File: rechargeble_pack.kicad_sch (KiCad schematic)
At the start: 42 parts, among them J1 Out, J2 LiPo, J3 DC IN, Q1 IRLML6402, Q2 BC857, Q6 BC847, Q7 BC857, U1 TP4056, U2 TPS61041

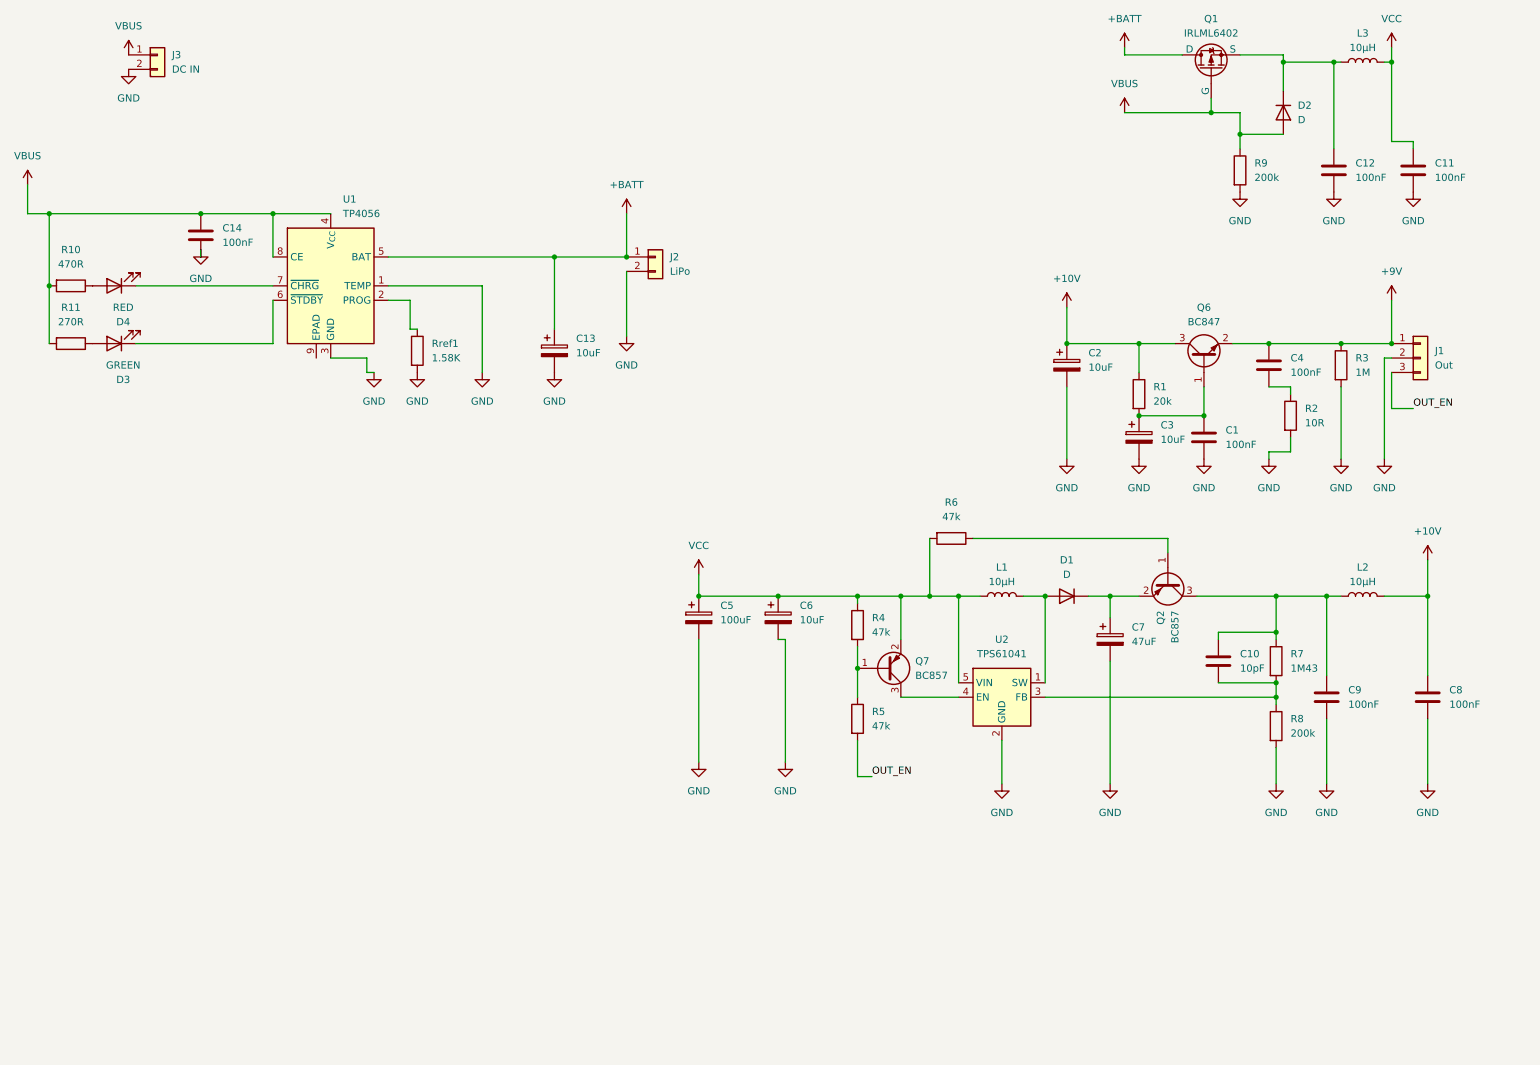
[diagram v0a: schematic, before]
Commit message: v3 redesign: 31x19 mm one-sided board, regulated 9.0 V, single LED
- Charger TP4057 (500 mA), power-path removed, MLCC instead of tantalum
- Boost TPS61041 at 11.5 V with output disconnect (Q2), EN pull-down fix
- Output chain: RC -> capacitance multiplier -> TPS7A4901 ultra-low-noise LDO, 9.02 V
- Single red/green LED: charging / charged / blinking low-battery (TLV3012)
- USB-C input TVS, project symbol library, JLC basic parts where possible
- New layout 31x19 mm, 2 layers, all SMD on top, ABYSS logo on bottom silk
- production/: gerbers, BOM+CPL for JLCPCB and PCBWay
- README rewritten, .gitignore added, v1 gerbers/BOM/CPL, KiCad backups and caches removed

Co-Authored-By: Claude Opus 5.5 <noreply@anthropic.com>
Claude-Session: https://claude.ai/code/session_01MaiZSNzApBdaqcYQCa8rQi
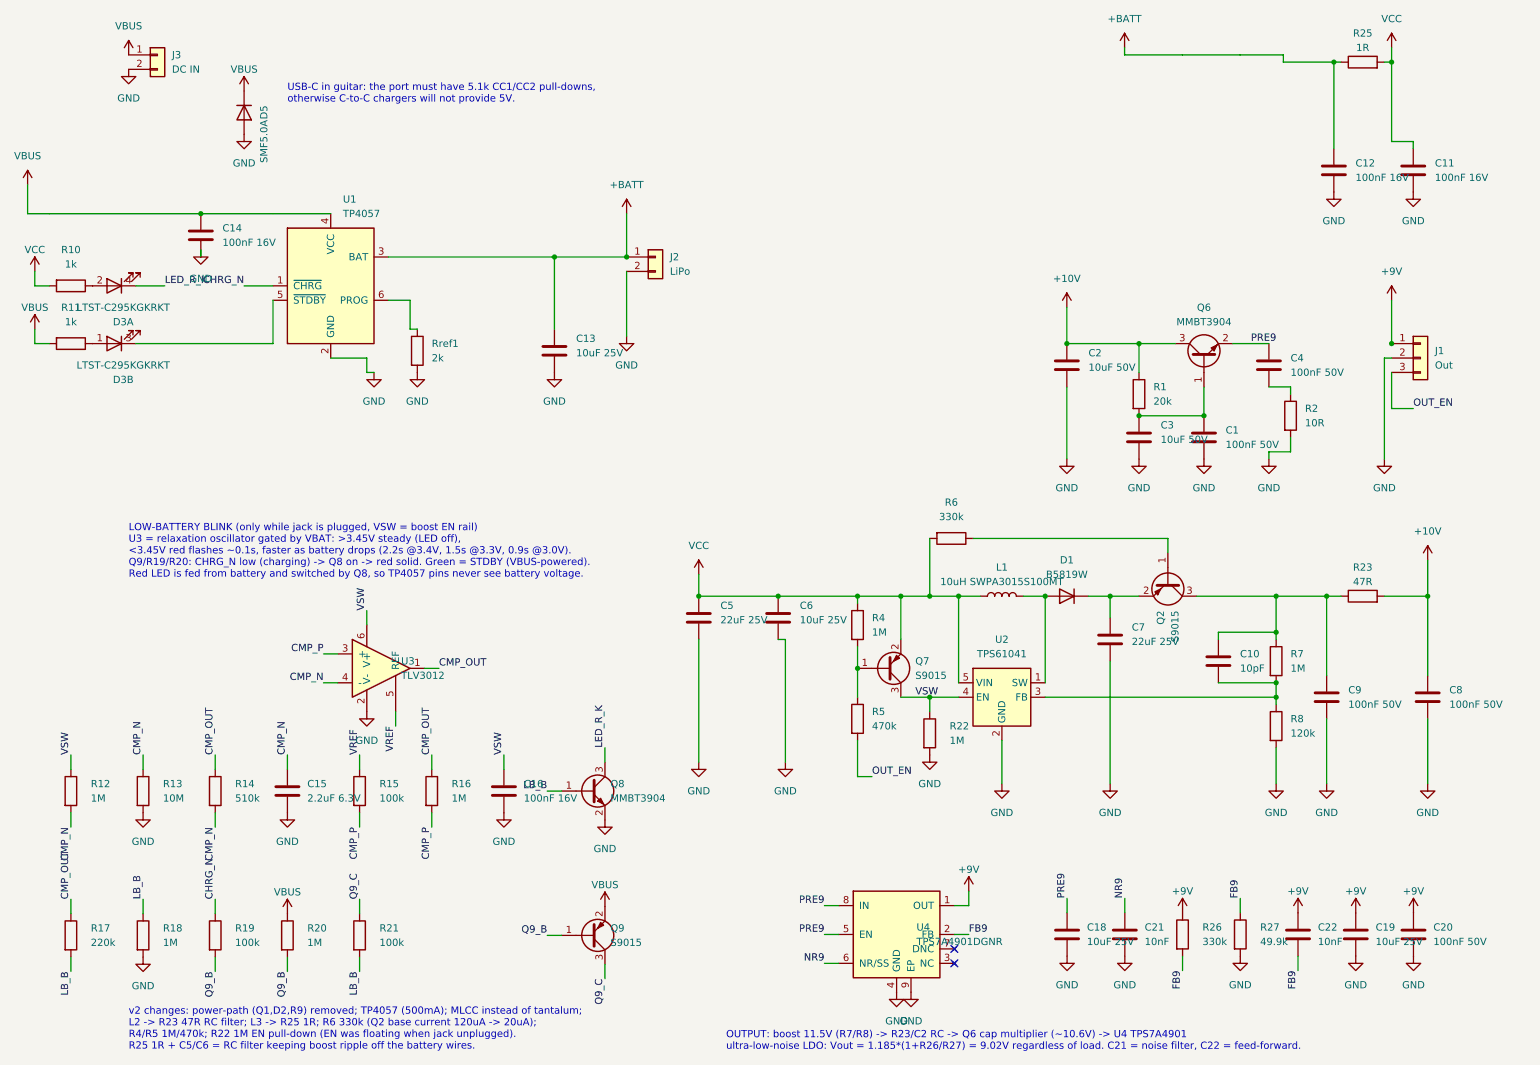
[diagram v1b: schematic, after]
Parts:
- removed D2: D, Diode_SMD:D_0805_2012Metric, symbol Device:D
- removed Q1: IRLML6402, Package_TO_SOT_SMD:SOT-23, symbol Simulation_SPICE:PMOS
- removed R3: 1M, Resistor_SMD:R_0805_2012Metric, symbol Device:R
- removed R9: 200k, Resistor_SMD:R_0805_2012Metric, symbol Device:R
- added C15: 2.2uF 6.3V, Capacitor_SMD:C_0402_1005Metric, symbol Device:C
- added C16: 100nF 16V, Capacitor_SMD:C_0402_1005Metric, symbol Device:C
- added C18, C19: 10uF 25V, Capacitor_SMD:C_0805_2012Metric, symbol Device:C
- added C20: 100nF 50V, Capacitor_SMD:C_0402_1005Metric, symbol Device:C
- added C21, C22: 10nF, Capacitor_SMD:C_0402_1005Metric, symbol Device:C
- added D5: SMF5.0A, Diode_SMD:D_SOD-123F, symbol Device:D
- added Q8: MMBT3904, Package_TO_SOT_SMD:SOT-23, symbol Transistor_BJT:BC847
- added Q9: S9015, Package_TO_SOT_SMD:SOT-23, symbol Transistor_BJT:BC857
- added R12, R16, R18, R20, R22: 1M, Resistor_SMD:R_0402_1005Metric, symbol Device:R
- added R13: 10M, Resistor_SMD:R_0402_1005Metric, symbol Device:R
- added R14: 510k, Resistor_SMD:R_0402_1005Metric, symbol Device:R
- added R15, R19, R21: 100k, Resistor_SMD:R_0402_1005Metric, symbol Device:R
- added R17: 220k, Resistor_SMD:R_0402_1005Metric, symbol Device:R
- added R26: 330k, Resistor_SMD:R_0402_1005Metric, symbol Device:R
- added R27: 49.9k, Resistor_SMD:R_0402_1005Metric, symbol Device:R
- added U3: TLV3012, Package_TO_SOT_SMD:SOT-23-6, symbol active_pu:TLV3012
- added U4: TPS7A4901DGNR, Package_SO:Texas_DGN0008D_VSSOP-8-1EP_3x3mm_P0.65mm_EP2x2.94mm_Mask1.57x1.89mm, symbol active_pu:TPS7A4901
- C1, C4, C8, C9: value 100nF -> 100nF 50V; footprint Capacitor_SMD:C_0805_2012Metric -> Capacitor_SMD:C_0402_1005Metric; LCSC (none) -> C307331
- C10: LCSC (none) -> C32949
- C11, C12, C14: value 100nF -> 100nF 16V; footprint Capacitor_SMD:C_0805_2012Metric -> Capacitor_SMD:C_0402_1005Metric; LCSC (none) -> C1525
- C13, C6: value 10uF -> 10uF 25V; footprint Capacitor_Tantalum_SMD:CP_EIA-3216-10_Kemet-I -> Capacitor_SMD:C_0805_2012Metric; symbol Device:C_Polarized -> Device:C; LCSC (none) -> C15850
- C2, C3: value 10uF -> 10uF 50V; footprint Capacitor_Tantalum_SMD:CP_EIA-3216-10_Kemet-I -> Capacitor_SMD:C_0805_2012Metric; symbol Device:C_Polarized -> Device:C; LCSC (none) -> C440198
- C5: value 100uF -> 22uF 25V; footprint Capacitor_Tantalum_SMD:CP_EIA-7343-15_Kemet-W -> Capacitor_SMD:C_0805_2012Metric; symbol Device:C_Polarized -> Device:C; LCSC (none) -> C45783
- C7: value 47uF -> 22uF 25V; footprint Capacitor_Tantalum_SMD:CP_EIA-3528-12_Kemet-T -> Capacitor_SMD:C_1206_3216Metric; symbol Device:C_Polarized -> Device:C; LCSC (none) -> C12891
- D1: value D -> B5819W; footprint Diode_SMD:D_0805_2012Metric -> Diode_SMD:D_SOD-123; LCSC (none) -> C8598
- D3: value GREEN -> LTST-C295KGKRKT; footprint LED_SMD:LED_0805_2012Metric -> LED_SMD:LED_LiteOn_LTST-C295K_1.6x0.8mm; symbol Device:LED -> active_pu:LED_Dual_RG; LCSC (none) -> C364568
- D3: renamed from D4; value RED -> LTST-C295KGKRKT; footprint LED_SMD:LED_0805_2012Metric -> LED_SMD:LED_LiteOn_LTST-C295K_1.6x0.8mm; symbol Device:LED -> active_pu:LED_Dual_RG; LCSC (none) -> C364568
- J1: footprint Connector_Wire:SolderWire-0.5sqmm_1x03_P4.8mm_D0.9mm_OD2.3mm -> Connector_PinHeader_2.54mm:PinHeader_1x03_P2.54mm_Vertical
- J2, J3: footprint Connector_Wire:SolderWire-0.5sqmm_1x02_P4.8mm_D0.9mm_OD2.3mm -> Connector_PinHeader_2.54mm:PinHeader_1x02_P2.54mm_Vertical
- L1: value 10µH -> 10uH SWPA3015S100MT; footprint Inductor_SMD:L_0805_2012Metric -> Inductor_SMD:L_Sunlord_SWPA3015S; LCSC (none) -> C45403
- Q2, Q7: value BC857 -> S9015; LCSC (none) -> C2149
- Q6: value BC847 -> MMBT3904; LCSC (none) -> C20526
- R1: footprint Resistor_SMD:R_0805_2012Metric -> Resistor_SMD:R_0402_1005Metric; LCSC (none) -> C25765
- R10: value 470R -> 1k; footprint Resistor_SMD:R_0805_2012Metric -> Resistor_SMD:R_0402_1005Metric; LCSC (none) -> C11702
- R11: value 270R -> 1k; footprint Resistor_SMD:R_0805_2012Metric -> Resistor_SMD:R_0402_1005Metric; LCSC (none) -> C11702
- R2: footprint Resistor_SMD:R_0805_2012Metric -> Resistor_SMD:R_0402_1005Metric; LCSC (none) -> C25077
- R23: renamed from L2; value 10µH -> 47R; footprint Inductor_SMD:L_0805_2012Metric -> Resistor_SMD:R_0402_1005Metric; symbol Device:L -> Device:R; LCSC (none) -> C25118
- R25: renamed from L3; value 10µH -> 1R; footprint Inductor_SMD:L_0805_2012Metric -> Resistor_SMD:R_0402_1005Metric; symbol Device:L -> Device:R; LCSC (none) -> C25086
- R4: value 47k -> 1M; footprint Resistor_SMD:R_0805_2012Metric -> Resistor_SMD:R_0402_1005Metric; LCSC (none) -> C26083
- R5: value 47k -> 470k; footprint Resistor_SMD:R_0805_2012Metric -> Resistor_SMD:R_0402_1005Metric; LCSC (none) -> C25790
- R6: value 47k -> 330k; footprint Resistor_SMD:R_0805_2012Metric -> Resistor_SMD:R_0402_1005Metric; LCSC (none) -> C25778
- R7: value 1M43 -> 1M; footprint Resistor_SMD:R_0805_2012Metric -> Resistor_SMD:R_0402_1005Metric; LCSC (none) -> C26083
- R8: value 200k -> 120k; footprint Resistor_SMD:R_0805_2012Metric -> Resistor_SMD:R_0402_1005Metric; LCSC (none) -> C25750
- Rref1: value 1.58K -> 2k; footprint Resistor_SMD:R_0805_2012Metric -> Resistor_SMD:R_0402_1005Metric; LCSC (none) -> C4109
- U1: value TP4056 -> TP4057; footprint Package_SO:SOIC-8-1EP_3.9x4.9mm_P1.27mm_EP2.41x3.3mm_ThermalVias -> Package_TO_SOT_SMD:SOT-23-6; symbol Battery_Management:TP4056-42-ESOP8 -> active_pu:TP4057; LCSC (none) -> C725791
- U2: LCSC (none) -> C9846
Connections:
- net +9V: now also C19.1, C20.1, C22.1, R26.1, U4.1 (OUT); no longer C4.1, Q6.2 (E)
- net +BATT: now also C12.1, R25.1, U1.3 (BAT); no longer U1.5 (BAT)
- net GND: now also U1.2 (GND), C15.2, C16.2, C18.2, C19.2, C20.2, C21.2, D5.2 (A), Q8.2 (E), R13.2, R18.2, R22.2, R27.2, U3.2 (V-), U4.4 (GND), U4.9 (EP); no longer U1.1 (TEMP), U1.3 (GND)
- net VBUS: now also D5.1 (K), Q9.2 (E), R20.1; no longer R10.2, U1.8 (CE)
- net VCC: now also R10.2
- net at Rref1.1: now also U1.6 (PROG); no longer U1.2 (PROG)
- net at R11.1: now also D3.1 (GA); no longer D3.2 (A)
- net VSW: now reaches Q7.3 (C), U2.4 (EN)
- net VSW: now also C16.1, R12.1, R22.1, U3.6 (V+)
- new net: D3.3 (GK), U1.5 (~{STDBY})
- new net CHRG_N: R19.1, U1.1 (~{CHRG})
- new net CMP_N: C15.1, R12.2, R13.1, R14.2, U3.4 (-)
- new net CMP_OUT: R14.1, R16.1, R17.1, U3.1
- new net CMP_P: R15.2, R16.2, U3.3 (+)
- new net FB9: C22.2, R26.2, R27.1, U4.2 (FB)
- new net LB_B: Q8.1 (B), R17.2, R18.1, R21.2
- new net LED_R_K: D3.4 (RK), Q8.3 (C)
- new net NR9: C21.1, U4.6 (NR/SS)
- new net PRE9: C18.1, C4.1, Q6.2 (E), U4.5 (EN), U4.8 (IN)
- new net Q9_B: Q9.1 (B), R19.2, R20.2
- new net Q9_C: Q9.3 (C), R21.1
- new net VREF: R15.1, U3.5 (REF)
- no-connect marks 0 -> 2
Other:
- note added: "LOW-BATTERY BLINK (only while jack is plugged, VSW = boost EN rail) U3 = relaxation oscillator gated by VBAT: >3.45V steady (LED off), <3.45V red flashes ~0.1s, faster as battery drops (2.2s @3.4V, 1.5s @3.3V, 0.9s @3.0V). Q9/R19/R20: CHRG_N low (charging) -> Q8 on -> red solid. Green = STDBY (VBUS-powered). Red LED is fed from battery and switched by Q8, so TP4057 pins never see battery voltage."
- note added: "OUTPUT: boost 11.5V (R7/R8) -> R23/C2 RC -> Q6 cap multiplier (~10.6V) -> U4 TPS7A4901 ultra-low-noise LDO: Vout = 1.185*(1+R26/R27) = 9.02V regardless of load. C21 = noise filter, C22 = feed-forward."
- note added: "USB-C in guitar: the port must have 5.1k CC1/CC2 pull-downs, otherwise C-to-C chargers will not provide 5V."
- note added: "v2 changes: power-path (Q1,D2,R9) removed; TP4057 (500mA); MLCC instead of tantalum; L2 -> R23 47R RC filter; L3 -> R25 1R; R6 330k (Q2 base current 120uA -> 20uA); R4/R5 1M/470k; R22 1M EN pull-down (EN was floating when jack unplugged). R25 1R + C5/C6 = RC filter keeping boost ripple off the battery wires."
